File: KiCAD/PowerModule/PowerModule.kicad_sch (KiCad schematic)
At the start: 0 parts

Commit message: 電池変更しました
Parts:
- added BT1, BT2, BT3, BT4, BT5: CR123A, TSRP_Battery:BHC-CR123A, symbol Device:Battery_Cell
- added C1, C10, C11, C13, C14, C4, C5, C6: 0.1uF, Capacitor_SMD:C_0603_1608Metric_Pad1.08x0.95mm_HandSolder, symbol Device:C_Small
- added C12, C8, C9: 10uF, Capacitor_SMD:C_1206_3216Metric_Pad1.33x1.80mm_HandSolder, symbol Device:C_Small
- added C16: 33uF, Capacitor_SMD:CP_Elec_6.3x5.9, symbol Device:C_Polarized_Small
- added C2, C3: 0.056uF, Capacitor_SMD:C_0603_1608Metric_Pad1.08x0.95mm_HandSolder, symbol Device:C_Small
- added C7: 2200uF, Capacitor_THT:CP_Radial_D18.0mm_P7.50mm, symbol Device:C_Polarized_Small
- added D1, D2: Orange, LED_SMD:LED_0603_1608Metric_Pad1.05x0.95mm_HandSolder, symbol Device:LED_Small
- added D3: SR54F, Diode_SMD:D_SMB_Handsoldering, symbol Device:D_Schottky
- added D4, D5, D6: GS1010FL, Diode_SMD:D_SOD-123F, symbol Device:D_Small
- added D7: Green, LED_SMD:LED_0603_1608Metric_Pad1.05x0.95mm_HandSolder, symbol Device:LED_Small
- added J1: GPU, Hirose_Connector:Hirose_DF1B, symbol Connector_Generic:Conn_01x02
- added J2: BATTERY, TSRP_Connector_Hirose:DF51-2P-2DS, symbol Connector_Generic:Conn_01x02
- added J3: BUS, TSRP_Connector_Hirose:DF51A-8DP-2DS, symbol Connector_Generic:Conn_01x08
- added J4: MONITOR, TSRP_Connector_Hirose:DF51A-8DP-2DS, symbol Connector_Generic:Conn_01x08
- added J5: MASTER, Hirose_Connector:Hirose_DF1B, symbol Connector_Generic:Conn_01x02
- added Q1, Q2: TK8S06K3L, Package_TO_SOT_SMD:TO-252-2, symbol Transistor_FET:QM6006D
- added Q3, Q5: AO3401A, Package_TO_SOT_SMD:SOT-23, symbol Transistor_FET:QM6015D
- added R1, R2, R7: 2.7kR, Resistor_SMD:R_0603_1608Metric_Pad0.98x0.95mm_HandSolder, symbol Device:R_Small
- added R13, R14, R15, R16: 10kR, Resistor_SMD:R_0603_1608Metric_Pad0.98x0.95mm_HandSolder, symbol Device:R
- added R17, R6: 5.6kR, Resistor_SMD:R_0603_1608Metric_Pad0.98x0.95mm_HandSolder, symbol Device:R_Small
- added R18: 3.3kR, Resistor_SMD:R_0603_1608Metric_Pad0.98x0.95mm_HandSolder, symbol Device:R_Small
- added R19, R3, R4, R5: 0.1R, Resistor_SMD:R_2816_7142Metric_Pad3.20x4.45mm_HandSolder, symbol Device:R
- added TH1, TH2, TH3, TH4: 10kR, Resistor_SMD:R_0603_1608Metric_Pad0.98x0.95mm_HandSolder, symbol Device:Thermistor_NTC
- added U1: LTC4353, Package_SO:MSOP-16_3x4mm_P0.5mm, symbol TSRP_IC:LTC4353
- added U2, U3, U4, U8: INA219BxDCN, Package_TO_SOT_SMD:SOT-23-8, symbol Sensor_Energy:INA219BxDCN
- added U5, U6, U7: NJM7812SDL1, Package_TO_SOT_SMD:TO-252-2, symbol Regulator_Linear:L7812
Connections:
- new net: C16.1, D3.1 (K), Q1.2 (D), Q2.2 (D), Q3.3 (S), R1.2, R17.1, R2.2, R6.2, U1.10 (OUT1), U1.7 (OUT2)
- new net: C3.1, U1.11 (CPO1)
- new net: Q1.1 (G), U1.12 (GATE1)
- new net: C3.2, Q1.3 (S), R3.2, U1.13 (VIN1), U3.2 (IN-)
- new net: C1.2, U1.14 (VCC)
- new net: C2.2, Q2.3 (S), R19.2, U1.4 (VIN2), U2.2 (IN-)
- new net: Q2.1 (G), U1.5 (GATE2)
- new net: C2.1, U1.6 (CPO2)
- new net: D2.1 (K), U1.8 (ONST1)
- new net: D1.1 (K), U1.9 (ONST1)
- new net: D7.2 (A), R7.1
- new net: C7.1, D3.2 (A), R6.1
- new net: J1.2 (Pin_2), R3.1, U3.1 (IN+)
- new net: C10.2, C11.2, C13.2, D4.2 (A), D5.2 (A), D6.2 (A), R4.1, U5.3 (OUT), U6.3 (OUT), U7.3 (OUT), U8.1 (IN+)
- new net: BT1.2 (-), BT2.1 (+)
- new net: BT2.2 (-), BT3.1 (+)
- new net: BT1.1 (+), J2.1 (Pin_1)
- new net: D1.2 (A), R1.1
- new net: D2.2 (A), R2.1
- new net: J2.2 (Pin_2), R19.1, U2.1 (IN+)
- new net: J5.2 (Pin_2), R18.2
- new net: Q5.3 (S), R5.1, U4.1 (IN+)
- new net: C16.2, Q3.1 (G), Q5.1 (G), R17.2, R18.1
- new net: Q3.2 (D), Q5.2 (D)
- new net: J3.5 (Pin_5), J3.6 (Pin_6)
- new net: J3.7 (Pin_7), J3.8 (Pin_8)
- new net: BT4.2 (-), BT5.1 (+)
- new net: BT3.2 (-), BT4.1 (+)
- new net +12V: J3.1 (Pin_1), J3.2 (Pin_2), R4.2, R7.2, U8.2 (IN-)
- new net +3.3V: C14.2, C4.2, C5.2, C6.2, J4.1 (Pin_1), R13.1, R14.1, R15.1, R16.1, U2.4 (VS), U2.7 (A0), U3.4 (VS), U4.4 (VS), U4.8 (A1), U8.4 (VS), U8.7 (A0), U8.8 (A1)
- new net +VSW: C12.2, C8.2, C9.2, D4.1 (K), D5.1 (K), D6.1 (K), R5.2, U4.2 (IN-), U5.1 (IN), U6.1 (IN), U7.1 (IN)
- new net GND: BT5.2 (-), C1.1, C10.1, C11.1, C12.1, C13.1, C14.1, C4.1, C5.1, C6.1, C7.2, C8.1, C9.1, D7.1 (K), J1.1 (Pin_1), J3.3 (Pin_3), J3.4 (Pin_4), J4.2 (Pin_2), J5.1 (Pin_1), TH1.2, TH2.2, TH3.2, TH4.2, U1.1 (EN2), U1.15 (GND), U1.16 (EN1), U2.3 (GND), U2.8 (A1), U3.3 (GND), U3.7 (A0), U3.8 (A1), U4.3 (GND), U4.7 (A0), U5.2 (GND), U6.2 (GND), U7.2 (GND), U8.3 (GND)
- new net I2C_SCL: J4.4 (Pin_4), U2.5 (SCL), U3.5 (SCL), U4.5 (SCL), U8.5 (SCL)
- new net I2C_SDA: J4.3 (Pin_3), U2.6 (SDA), U3.6 (SDA), U4.6 (SDA), U8.6 (SDA)
- new net VREF_T1: J4.5 (Pin_5), R13.2, TH1.1
- new net VREF_T2: J4.6 (Pin_6), R14.2, TH2.1
- new net VREF_T3: J4.7 (Pin_7), R15.2, TH3.1
- new net VREF_T4: J4.8 (Pin_8), R16.2, TH4.1

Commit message: LTC3118の回路作ってみた
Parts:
- removed C1, C10, C11, C13: 0.1uF, Capacitor_SMD:C_0603_1608Metric_Pad1.08x0.95mm_HandSolder, symbol Device:C_Small
- removed C12, C8, C9: 10uF, Capacitor_SMD:C_1206_3216Metric_Pad1.33x1.80mm_HandSolder, symbol Device:C_Small
- removed C2, C3: 0.056uF, Capacitor_SMD:C_0603_1608Metric_Pad1.08x0.95mm_HandSolder, symbol Device:C_Small
- removed D4, D5, D6: GS1010FL, Diode_SMD:D_SOD-123F, symbol Device:D_Small
- removed Q1, Q2: TK8S06K3L, Package_TO_SOT_SMD:TO-252-2, symbol Transistor_FET:QM6006D
- removed R14, R15, R16: 10kR, Resistor_SMD:R_0603_1608Metric_Pad0.98x0.95mm_HandSolder, symbol Device:R
- removed TH2, TH3, TH4: 10kR, Resistor_SMD:R_0603_1608Metric_Pad0.98x0.95mm_HandSolder, symbol Device:Thermistor_NTC
- removed U1: LTC4353, Package_SO:MSOP-16_3x4mm_P0.5mm, symbol TSRP_IC:LTC4353
- removed U5, U6, U7: NJM7812SDL1, Package_TO_SOT_SMD:TO-252-2, symbol Regulator_Linear:L7812
- added C? (x2): 47uF, symbol Device:C
- added R8, R9, R?: 10k, symbol Device:R
- added R?: 301k, symbol Device:R
- added R?: 100k, symbol Device:R
- added R?: 200k, symbol Device:R
- added R?: 768k, symbol Device:R
- added U?: ~, symbol TSRP_IC:StrawberryLinux_LTC3118
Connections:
- net +VSW: now also R4.1, U8.1 (IN+)
- net GND: now also R?.2, R?.2, U?.1 (GND), U?.16 (GND), U?.17 (GND), U?.4 (GND), U?.5 (GND)
- net at R3.2, U3.2 (IN-): now also R?.1, U?.3 (VIN1)
- net at R19.2, U2.2 (IN-): now also R?.1, U?.2 (VIN2)
- net at D2.1 (K): now also C?.2
- net at D1.1 (K): now also C?.2
- new net: R?.1, R?.2, U?.7 (RUN2)
- new net: C?.1, U?.14 (VOUT)
- new net: C?.1, R8.1, R9.1, R?.1, U?.11 (PGD), U?.12 (V2GD), U?.13 (V1GD), U?.15 (VOUT)
- new net: R?.1, R?.2, U?.6 (RUN1)
- new net: U?.10 (SEL), U?.8 (VCC), U?.9 (MODE)
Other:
- moved on the sheet: C16, C4, C6, C7, D1, D2, D3, J5, Q3, Q5, R1, R17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

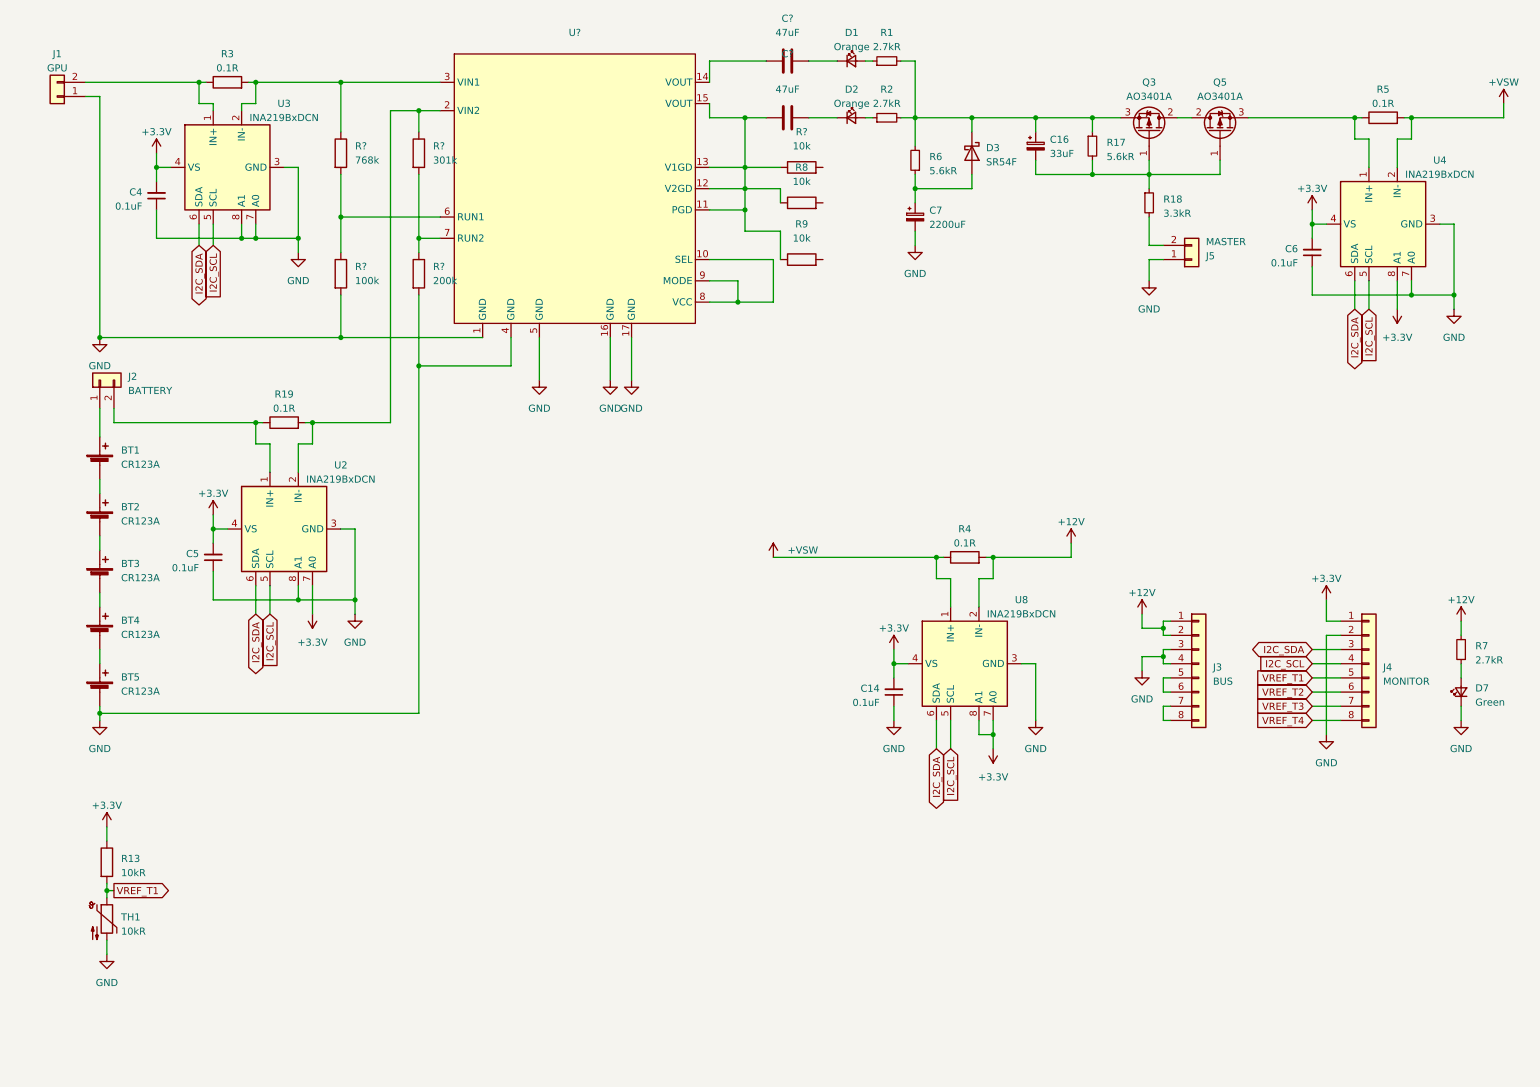
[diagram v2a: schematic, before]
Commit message: PowerGood変更しました
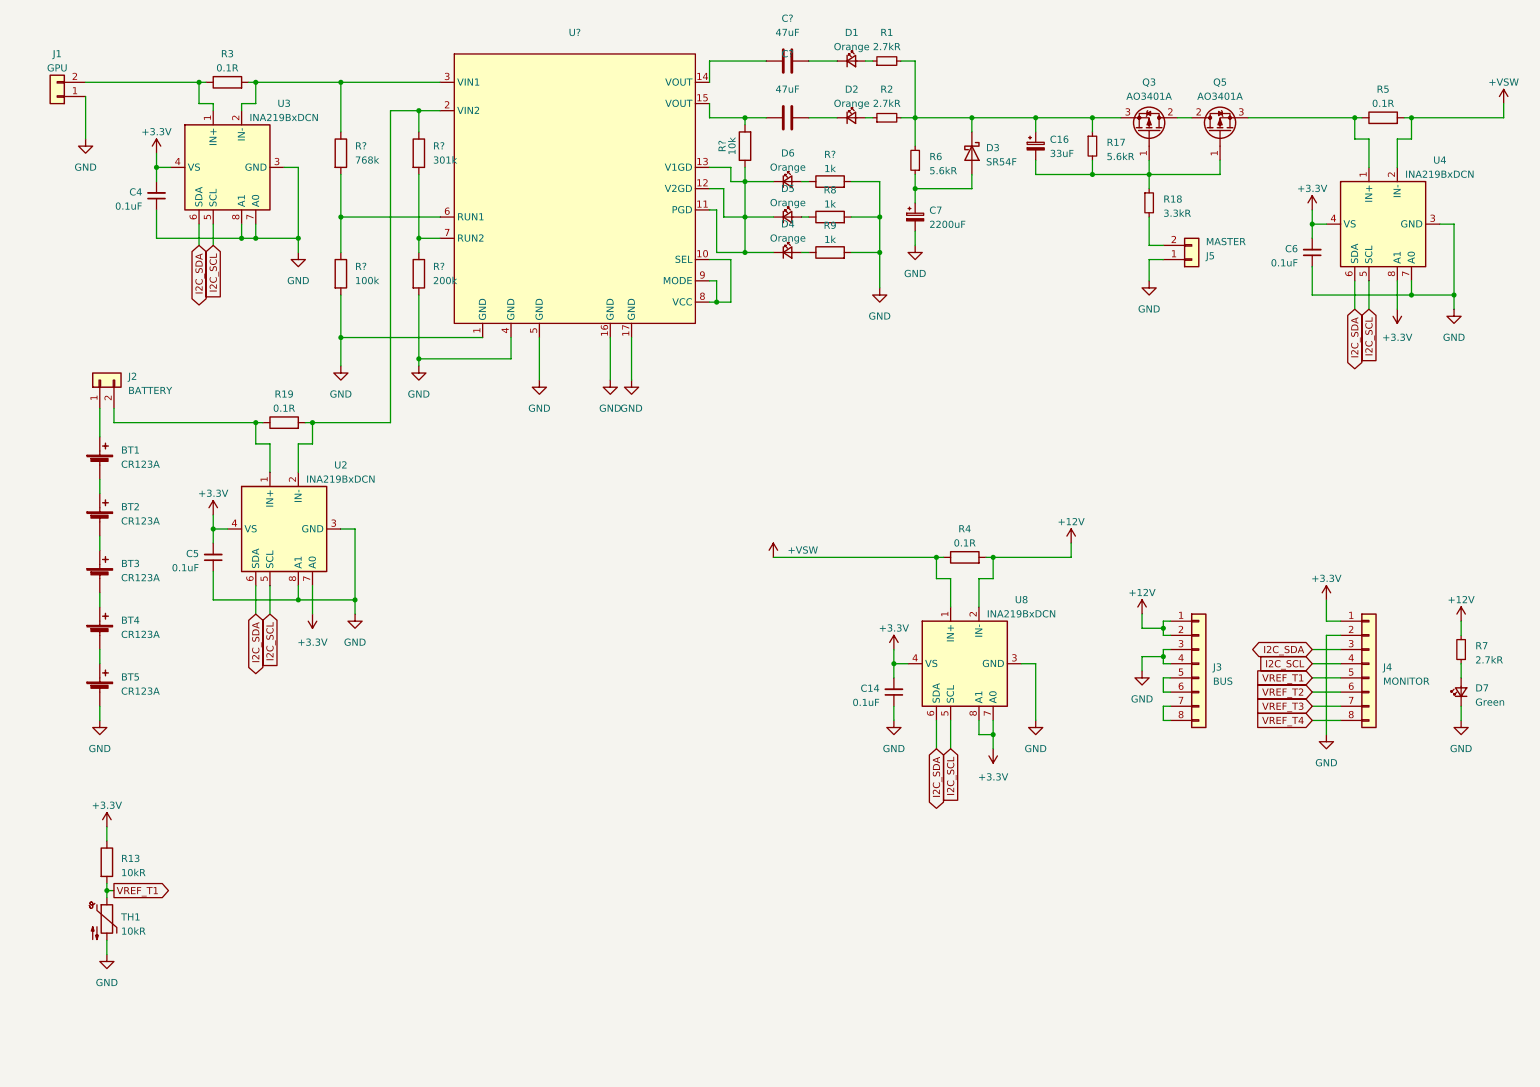
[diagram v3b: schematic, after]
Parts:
- added D4, D5, D6: Orange, LED_SMD:LED_0603_1608Metric_Pad1.05x0.95mm_HandSolder, symbol Device:LED_Small
- added R?: 1k, symbol Device:R
- R8, R9: value 10k -> 1k
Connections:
- net GND: now also R8.2, R9.2, R?.2
- net at R?.1, U?.11 (PGD), U?.12 (V2GD)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: now also D4.1 (K), D5.1 (K), D6.1 (K); no longer C?.1, R8.1, R9.1, U?.15 (VOUT)
- net at R?.2: now also C?.1, U?.15 (VOUT)
- new net: D6.2 (A), R?.1
- new net: D5.2 (A), R8.1
- new net: D4.2 (A), R9.1
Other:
- moved on the sheet: R?

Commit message: BatteryModule追加＆電池設置
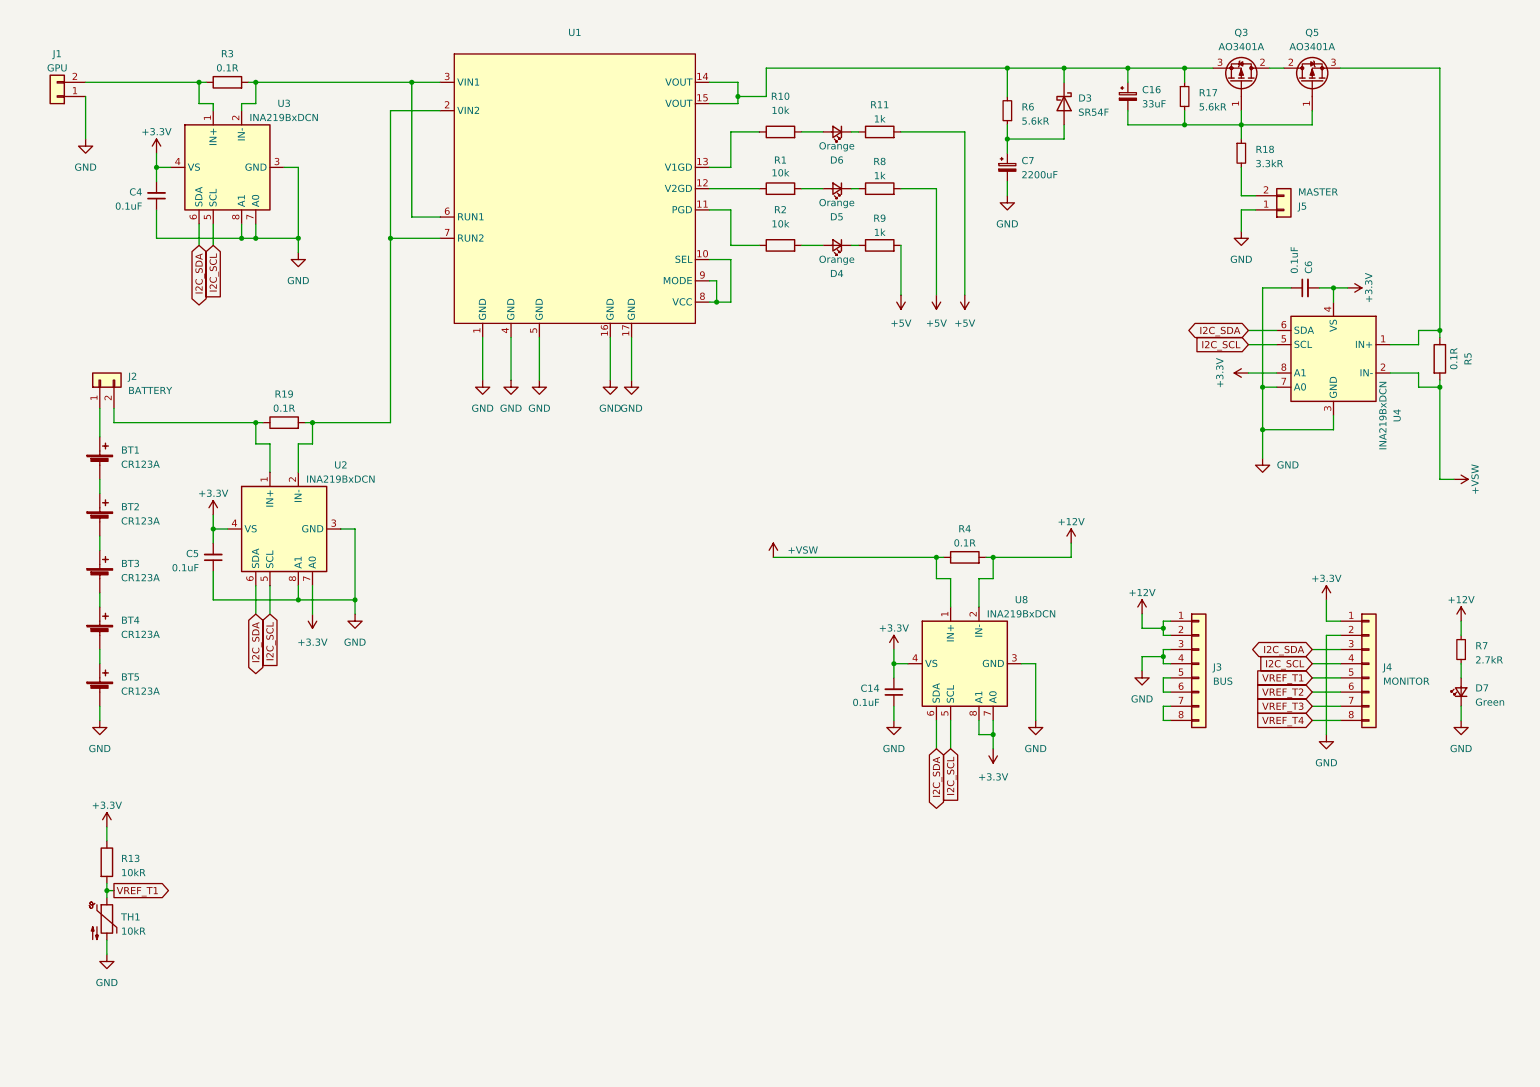
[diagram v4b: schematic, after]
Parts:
- removed C? (x2): 47uF, symbol Device:C
- removed D1, D2: Orange, LED_SMD:LED_0603_1608Metric_Pad1.05x0.95mm_HandSolder, symbol Device:LED_Small
- removed R1, R2: 2.7kR, Resistor_SMD:R_0603_1608Metric_Pad0.98x0.95mm_HandSolder, symbol Device:R_Small
- removed R?: 301k, symbol Device:R
- removed R?: 10k, symbol Device:R
- removed R?: 100k, symbol Device:R
- removed R?: 200k, symbol Device:R
- removed R?: 768k, symbol Device:R
- added R1, R10, R2: 10k, symbol Device:R
- J1, J5: footprint Hirose_Connector:Hirose_DF1B -> TSRP_Connector_Hirose:DF1B-2S-2.5R
- J2: footprint TSRP_Connector_Hirose:DF51-2P-2DS -> TSRP_Connector_Hirose:DF1B-2S-2.5R
- J3, J4: footprint TSRP_Connector_Hirose:DF51A-8DP-2DS -> TSRP_Connector_Hirose:DF11-8DP-2DS
- U1: renamed from U?; footprint (none) -> TSRP_IC:StrawberryLinux_LTC3118
- gave numbers to parts that had none: 1
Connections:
- net GND: no longer R11.2, R8.2, R9.2
- net at R19.2, U1.2 (VIN2), U2.2 (IN-): now also U1.7 (RUN2)
- net at R11.1: now also D6.1 (K); no longer D6.2 (A)
- net at U1.14 (VOUT): now also C16.1, D3.1 (K), Q3.3 (S), R17.1, R6.2, U1.15 (VOUT)
- net at R8.1: now also D5.1 (K); no longer D5.2 (A)
- net at U1.6 (RUN1): now also R3.2, U1.3 (VIN1), U3.2 (IN-)
- net at R9.1: now also D4.1 (K); no longer D4.2 (A)
- new net: D6.2 (A), R10.2
- new net: R10.1, U1.13 (V1GD)
- new net: D4.2 (A), R2.2
- new net: D5.2 (A), R1.2
- new net: R1.1, U1.12 (V2GD)
- new net: R2.1, U1.11 (PGD)
- new net +5V: R11.2, R8.2, R9.2
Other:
- moved on the sheet: C16, C6, C7, D3, D4, D5, D6, J5, Q3, Q5, R11, R17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

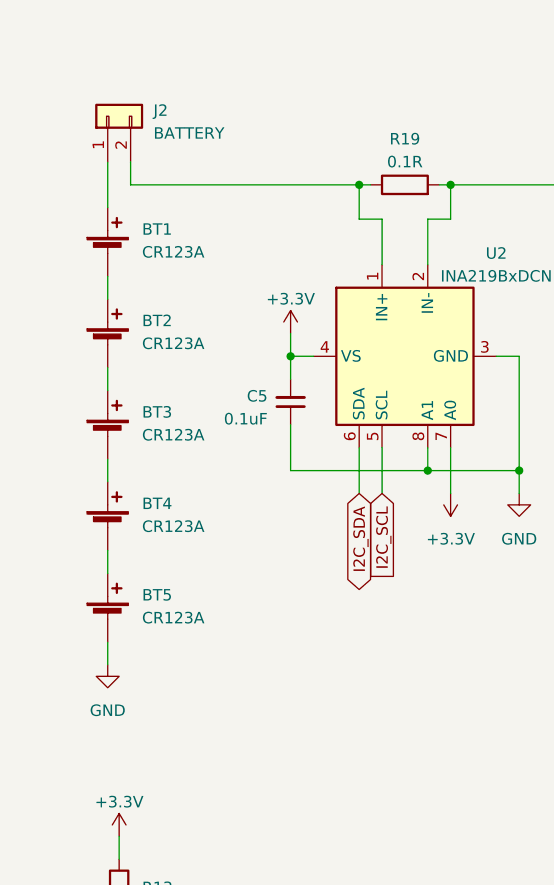
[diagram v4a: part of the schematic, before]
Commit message: PowerModule基板に収まりました。配線検討中
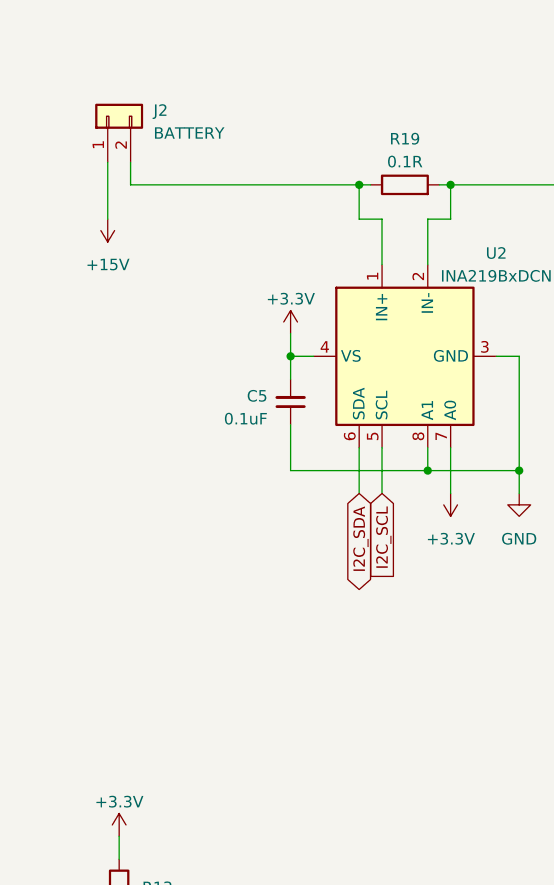
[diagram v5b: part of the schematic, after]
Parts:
- removed BT1, BT2, BT3, BT4, BT5: CR123A, TSRP_Battery:BHC-CR123A, symbol Device:Battery_Cell
- R1, R10, R11, R2, R8, R9: footprint (none) -> Resistor_SMD:R_0603_1608Metric
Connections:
- net +15V: now reaches J2.1 (Pin_1)

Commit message: 配線の確認お願いします
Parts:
- removed C14: 0.1uF, Capacitor_SMD:C_0603_1608Metric_Pad1.08x0.95mm_HandSolder, symbol Device:C_Small
- removed R4: 0.1R, Resistor_SMD:R_2816_7142Metric_Pad3.20x4.45mm_HandSolder, symbol Device:R
- removed U8: INA219BxDCN, Package_TO_SOT_SMD:SOT-23-8, symbol Sensor_Energy:INA219BxDCN
- added J6: Conn_01x02, TSRP_Connector_Hirose:DF1B-2S-2.5R, symbol Connector_Generic:Conn_01x02
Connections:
- net +VSW is gone; now on net +12V: R5.2, U4.2 (IN-)
- net GND: now also J6.1 (Pin_1)
- net +15V: no longer names the net of J2.1 (Pin_1)
- net +15V: now also J6.2 (Pin_2)
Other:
- moved on the sheet: J2

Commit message: 配線完了
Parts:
- removed C7: 2200uF, Capacitor_THT:CP_Radial_D18.0mm_P7.50mm, symbol Device:C_Polarized_Small
- added H1, H2, H3, H4: MountingHole, MountingHole:MountingHole_3.2mm_M3_DIN965_Pad_TopBottom, symbol Mechanical:MountingHole
- added J7: Conn_01x02, TSRP_Connector_Hirose:DF1B-2S-2.5R, symbol Connector_Generic:Conn_01x02
- TH1: footprint Resistor_SMD:R_0603_1608Metric_Pad0.98x0.95mm_HandSolder -> Connector_PinHeader_1.00mm:PinHeader_1x02_P1.00mm_Vertical
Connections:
- net at D3.2 (A), R6.1: now also J7.1 (Pin_1)
- no-connect marks 0 -> 1
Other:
- note added: "BatteryModule"
